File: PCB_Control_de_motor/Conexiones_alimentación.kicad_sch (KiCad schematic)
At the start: 9 parts, among them IC3 AP63203WU-7

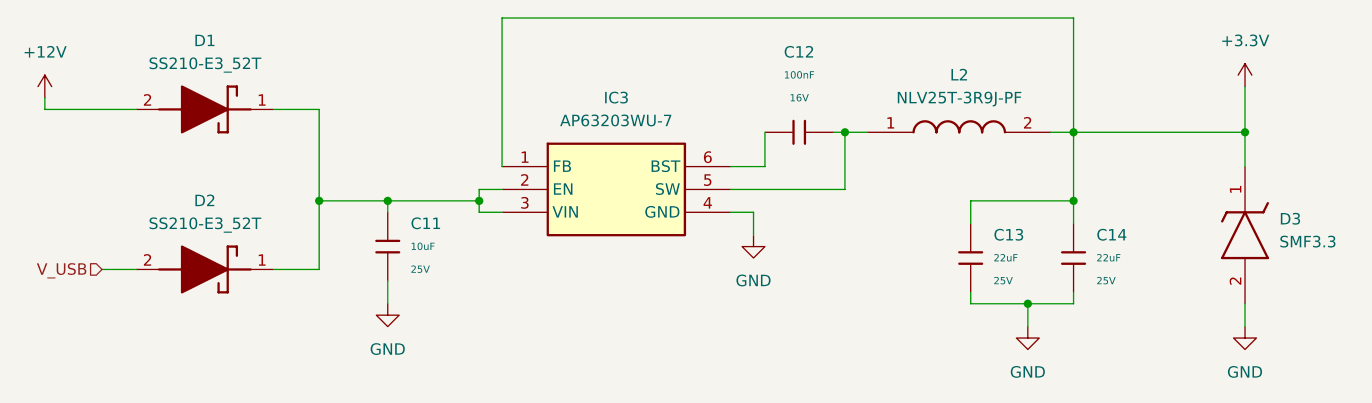
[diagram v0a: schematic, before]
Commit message: Corrección 3 del esquemático
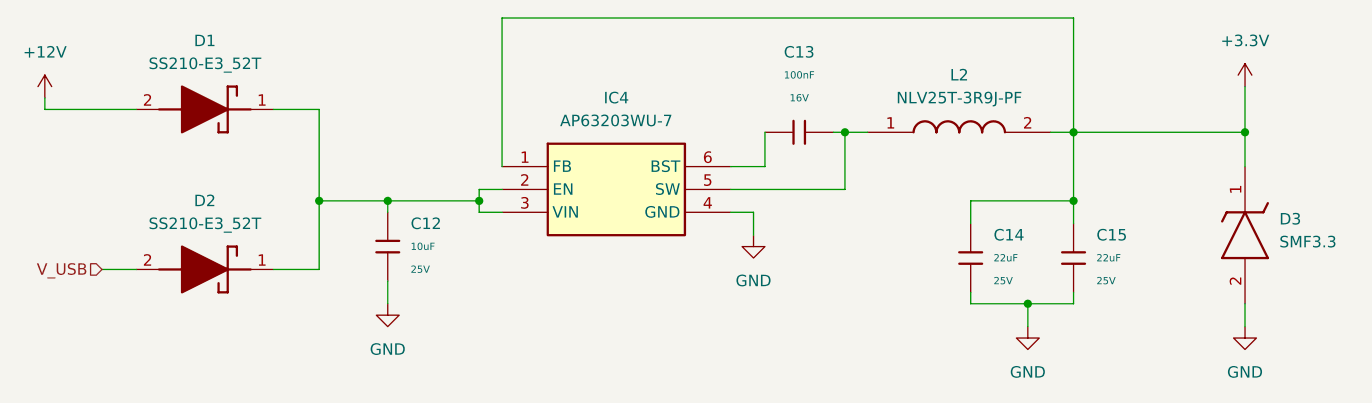
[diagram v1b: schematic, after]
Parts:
- D1, D2: footprint DIONM5436X244N -> SamacSys_Parts:DIONM5436X244N
- D3: footprint SOD3718X108N -> SamacSys_Parts:SOD3718X108N
- renumbered C11 to C12, C12 to C13, C13 to C14, C14 to C15, IC3 to IC4
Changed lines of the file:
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@@
 		(dnp no)
 		(fields_autoplaced yes)
-		(property "Reference" "C11"
+		(property "Reference" "C12"
 			(at 109.22 78.7399 0)
 			(effects
@@
 			(project ""
 				(path "/8d17a2c0-3da6-4d80-8f2f-d7746ccde60e/6944256d-9abd-4a40-876b-acdeed9558be"
-					(reference "C11")
+					(reference "C12")
 					(unit 1)
 				)
@@
 		(dnp no)
 		(fields_autoplaced yes)
-		(property "Reference" "C13"
+		(property "Reference" "C14"
 			(at 173.99 80.0099 0)
 			(effects
@@
 			(project ""
 				(path "/8d17a2c0-3da6-4d80-8f2f-d7746ccde60e/6944256d-9abd-4a40-876b-acdeed9558be"
-					(reference "C13")
+					(reference "C14")
 					(unit 1)
 				)
@@
 		(dnp no)
 		(fields_autoplaced yes)
-		(property "Reference" "IC3"
+		(property "Reference" "IC4"
 			(at 132.08 64.77 0)
 			(effects
@@
 			(project ""
 				(path "/8d17a2c0-3da6-4d80-8f2f-d7746ccde60e/6944256d-9abd-4a40-876b-acdeed9558be"
-					(reference "IC3")
+					(reference "IC4")
 					(unit 1)
 				)
@@
 			)
 		)
-		(property "Footprint" "DIONM5436X244N"
+		(property "Footprint" "SamacSys_Parts:DIONM5436X244N"
 			(at 83.82 -27.61 0)
 			(effects
@@
 			)
 		)
-		(property "Footprint" "SOD3718X108N"
+		(property "Footprint" "SamacSys_Parts:SOD3718X108N"
 			(at 108.28 82.55 0)
 			(effects
@@
 		(dnp no)
 		(fields_autoplaced yes)
-		(property "Reference" "C12"
+		(property "Reference" "C13"
 			(at 152.4 59.69 90)
 			(effects
@@
 			(project ""
 				(path "/8d17a2c0-3da6-4d80-8f2f-d7746ccde60e/6944256d-9abd-4a40-876b-acdeed9558be"
-					(reference "C12")
+					(reference "C13")
 					(unit 1)
 				)
@@
 			)
 		)
-		(property "Footprint" "DIONM5436X244N"
+		(property "Footprint" "SamacSys_Parts:DIONM5436X244N"
 			(at 83.82 -9.83 0)
 			(effects
@@
 		(dnp no)
 		(fields_autoplaced yes)
-		(property "Reference" "C14"
+		(property "Reference" "C15"
 			(at 185.42 80.0099 0)
 			(effects
@@
 			(project "PCB_Control_de_motor"
 				(path "/8d17a2c0-3da6-4d80-8f2f-d7746ccde60e/6944256d-9abd-4a40-876b-acdeed9558be"
-					(reference "C14")
+					(reference "C15")
 					(unit 1)
 				)

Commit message: Agregado de diodos TVS y avance del PCB con fuente y micro listo
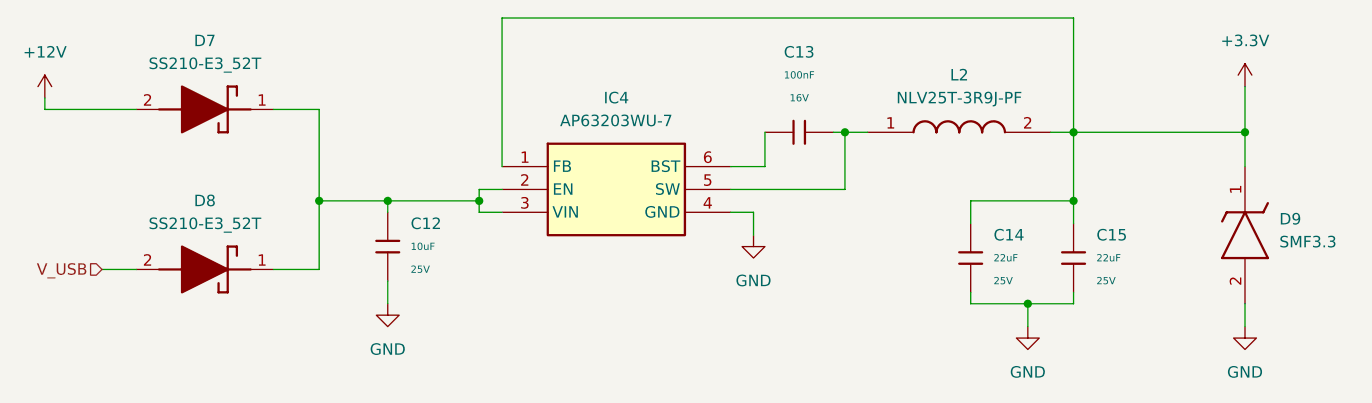
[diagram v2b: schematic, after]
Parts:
- renumbered D1 to D7, D2 to D8, D3 to D9
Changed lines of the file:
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@@
 		(dnp no)
 		(fields_autoplaced yes)
-		(property "Reference" "#PWR034"
+		(property "Reference" "#PWR039"
 			(at 177.8 96.52 0)
 			(effects
@@
 			(project "PCB_Control_de_motor"
 				(path "/8d17a2c0-3da6-4d80-8f2f-d7746ccde60e/6944256d-9abd-4a40-876b-acdeed9558be"
-					(reference "#PWR034")
+					(reference "#PWR039")
 					(unit 1)
 				)
@@
 		(dnp no)
 		(fields_autoplaced yes)
-		(property "Reference" "#PWR036"
+		(property "Reference" "#PWR041"
 			(at 201.93 96.52 0)
 			(effects
@@
 			(project "PCB_Control_de_motor"
 				(path "/8d17a2c0-3da6-4d80-8f2f-d7746ccde60e/6944256d-9abd-4a40-876b-acdeed9558be"
-					(reference "#PWR036")
+					(reference "#PWR041")
 					(unit 1)
 				)
@@
 		(dnp no)
 		(fields_autoplaced yes)
-		(property "Reference" "#PWR031"
+		(property "Reference" "#PWR036"
 			(at 68.58 68.58 0)
 			(effects
@@
 			(project ""
 				(path "/8d17a2c0-3da6-4d80-8f2f-d7746ccde60e/6944256d-9abd-4a40-876b-acdeed9558be"
-					(reference "#PWR031")
+					(reference "#PWR036")
 					(unit 1)
 				)
@@
 		(dnp no)
 		(fields_autoplaced yes)
-		(property "Reference" "#PWR032"
+		(property "Reference" "#PWR037"
 			(at 106.68 93.98 0)
 			(effects
@@
 			(project ""
 				(path "/8d17a2c0-3da6-4d80-8f2f-d7746ccde60e/6944256d-9abd-4a40-876b-acdeed9558be"
-					(reference "#PWR032")
+					(reference "#PWR037")
 					(unit 1)
 				)
@@
 		(dnp no)
 		(fields_autoplaced yes)
-		(property "Reference" "#PWR035"
+		(property "Reference" "#PWR040"
 			(at 201.93 67.31 0)
 			(effects
@@
 			(project ""
 				(path "/8d17a2c0-3da6-4d80-8f2f-d7746ccde60e/6944256d-9abd-4a40-876b-acdeed9558be"
-					(reference "#PWR035")
+					(reference "#PWR040")
 					(unit 1)
 				)
@@
 		(dnp no)
 		(fields_autoplaced yes)
-		(property "Reference" "D1"
+		(property "Reference" "D7"
 			(at 86.36 58.42 0)
 			(effects
@@
 			(project ""
 				(path "/8d17a2c0-3da6-4d80-8f2f-d7746ccde60e/6944256d-9abd-4a40-876b-acdeed9558be"
-					(reference "D1")
+					(reference "D7")
 					(unit 1)
 				)
@@
 		(dnp no)
 		(fields_autoplaced yes)
-		(property "Reference" "D3"
+		(property "Reference" "D9"
 			(at 205.74 78.2319 90)
 			(effects
@@
 			(project ""
 				(path "/8d17a2c0-3da6-4d80-8f2f-d7746ccde60e/6944256d-9abd-4a40-876b-acdeed9558be"
-					(reference "D3")
+					(reference "D9")
 					(unit 1)
 				)
@@
 		(dnp no)
 		(fields_autoplaced yes)
-		(property "Reference" "#PWR033"
+		(property "Reference" "#PWR038"
 			(at 147.32 86.36 0)
 			(effects
@@
 			(project "PCB_Control_de_motor"
 				(path "/8d17a2c0-3da6-4d80-8f2f-d7746ccde60e/6944256d-9abd-4a40-876b-acdeed9558be"
-					(reference "#PWR033")
+					(reference "#PWR038")
 					(unit 1)
 				)
@@
 		(dnp no)
 		(fields_autoplaced yes)
-		(property "Reference" "D2"
+		(property "Reference" "D8"
 			(at 86.36 76.2 0)
 			(effects
@@
 			(project "PCB_Control_de_motor"
 				(path "/8d17a2c0-3da6-4d80-8f2f-d7746ccde60e/6944256d-9abd-4a40-876b-acdeed9558be"
-					(reference "D2")
+					(reference "D8")
 					(unit 1)
 				)
